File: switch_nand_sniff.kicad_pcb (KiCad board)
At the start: 2 copper layers, 24.9 x 11.4 mm, 7 parts, among them P1 CONN_02X15, P2 CONN_02X15, P3 CONN_01X02, P4 CONN_01X02

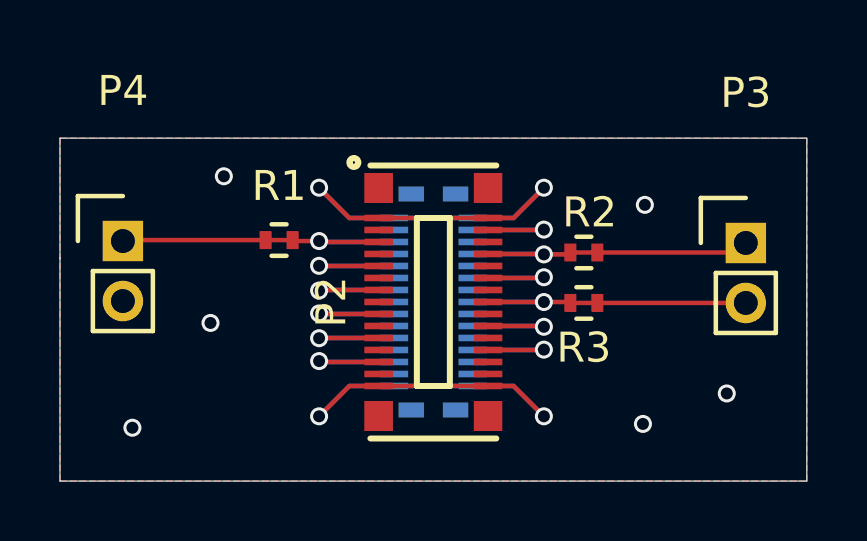
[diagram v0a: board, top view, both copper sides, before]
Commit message: Rev 1.1. Fixed resistor pad sizes, added thermal relief for ground plane.
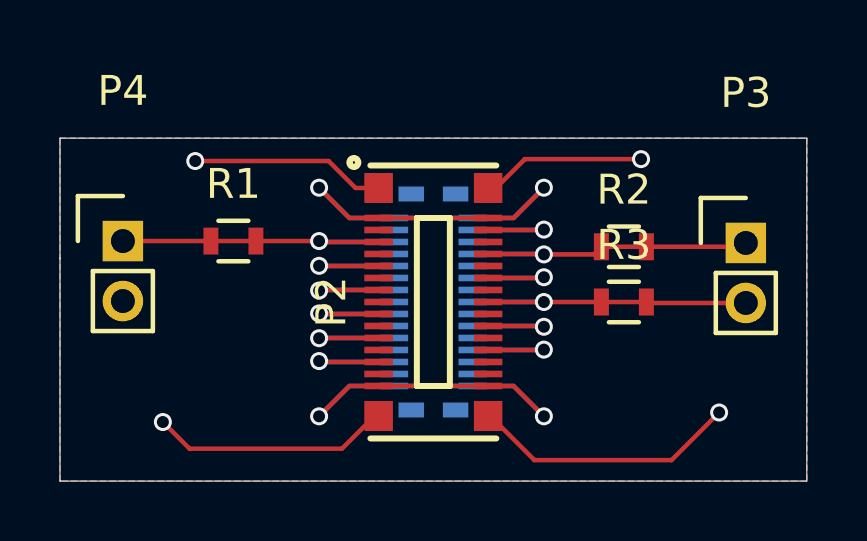
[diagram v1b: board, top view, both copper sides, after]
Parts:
- R1, R2, R3: footprint Resistors_SMD:R_0402 -> Resistors_SMD:R_0603
- moved R1 1.52 mm to (128.3, 133.0)
- moved R2 1.35 mm to (141.4, 133.2)
- moved R3 1.33 mm to (141.4, 135.0)
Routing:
- net GND: track 0.00 -> 29.4 mm, vias 0 -> 4
- net (no net): vias 6 -> 0

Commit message: Add sip-8. staging before rollback to find resistor desired.
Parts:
- removed R1, R2, R3: 0 Ohms, Resistors_SMD:R_0603
- P3, P4: value CONN_01X02 -> CONN_01X08; footprint Pin_Headers:Pin_Header_Straight_1x02_Pitch2.00mm -> switch:SIP-8
- moved P4 18.4 mm to (135.8, 147.6)
- moved P3 15.2 mm to (134.0, 122.9)
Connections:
- P1 pad 31: GND -> (no net)
- P2 pad 31: GND -> (no net)
- P3 pad 1: Net-(P1-Pad27) -> GND
- P3 pad 2: Net-(P1-Pad23) -> Net-(P1-Pad7)
- P4 pad 1: Net-(P1-Pad3) -> GND
- P4 pad 2: GND -> Net-(P1-Pad9)
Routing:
- net GND: track 29.4 -> 0.00 mm, vias 4 -> 0
- net Net-(P1-Pad27): track 11.6 -> 4.24 mm
- net Net-(P1-Pad23): track 11.0 -> 4.23 mm
- net Net-(P1-Pad3): track 11.1 -> 4.50 mm
- net (no net): track 0.00 -> 0.92 mm

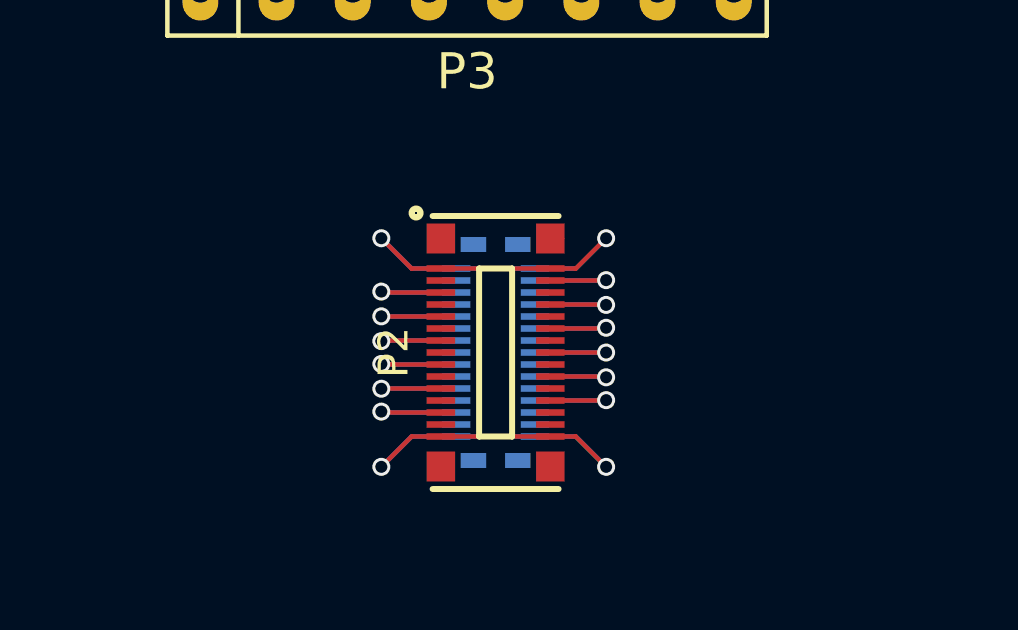
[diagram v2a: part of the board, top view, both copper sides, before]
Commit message: Added derefelection resistors, still needs matched-length routing.
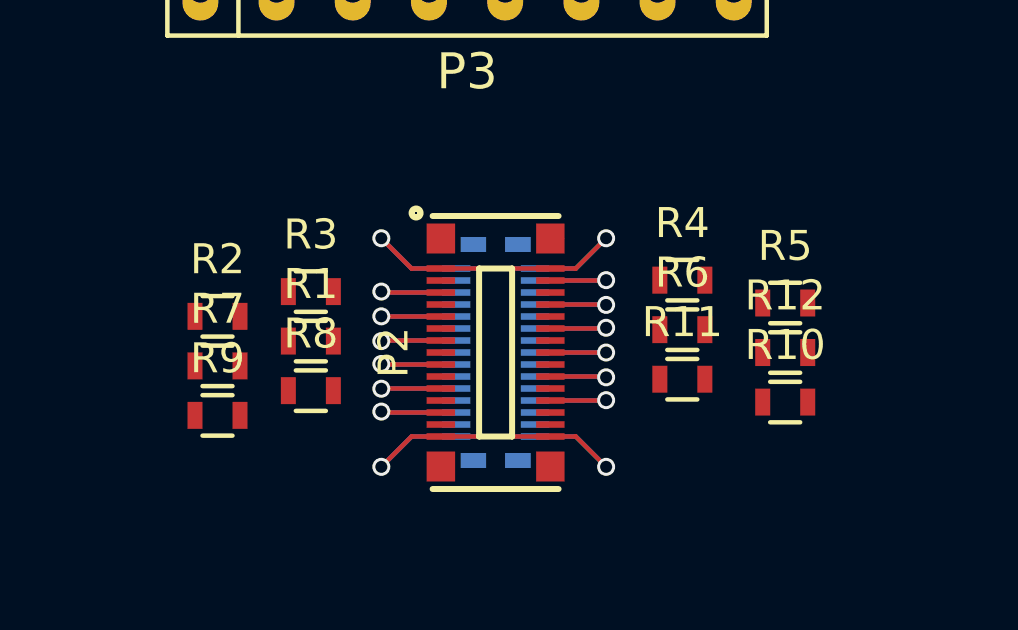
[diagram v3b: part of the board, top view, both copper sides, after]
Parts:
- added R1: 500 Ohms, Resistors_SMD:R_0603, F.Cu at (128.8, 134.6)
- added R10: 500 Ohms, Resistors_SMD:R_0603, F.Cu at (144.7, 136.7)
- added R11: 500 Ohms, Resistors_SMD:R_0603, F.Cu at (141.2, 135.9)
- added R12: 500 Ohms, Resistors_SMD:R_0603, F.Cu at (144.7, 135.0)
- added R2: 500 Ohms, Resistors_SMD:R_0603, F.Cu at (125.7, 133.8)
- added R3: 500 Ohms, Resistors_SMD:R_0603, F.Cu at (128.8, 133.0)
- added R4: 500 Ohms, Resistors_SMD:R_0603, F.Cu at (141.2, 132.6)
- added R5: 500 Ohms, Resistors_SMD:R_0603, F.Cu at (144.7, 133.3)
- added R6: 500 Ohms, Resistors_SMD:R_0603, F.Cu at (141.2, 134.2)
- added R7: 500 Ohms, Resistors_SMD:R_0603, F.Cu at (125.7, 135.4)
- added R8: 500 Ohms, Resistors_SMD:R_0603, F.Cu at (128.8, 136.3)
- added R9: 500 Ohms, Resistors_SMD:R_0603, F.Cu at (125.7, 137.1)

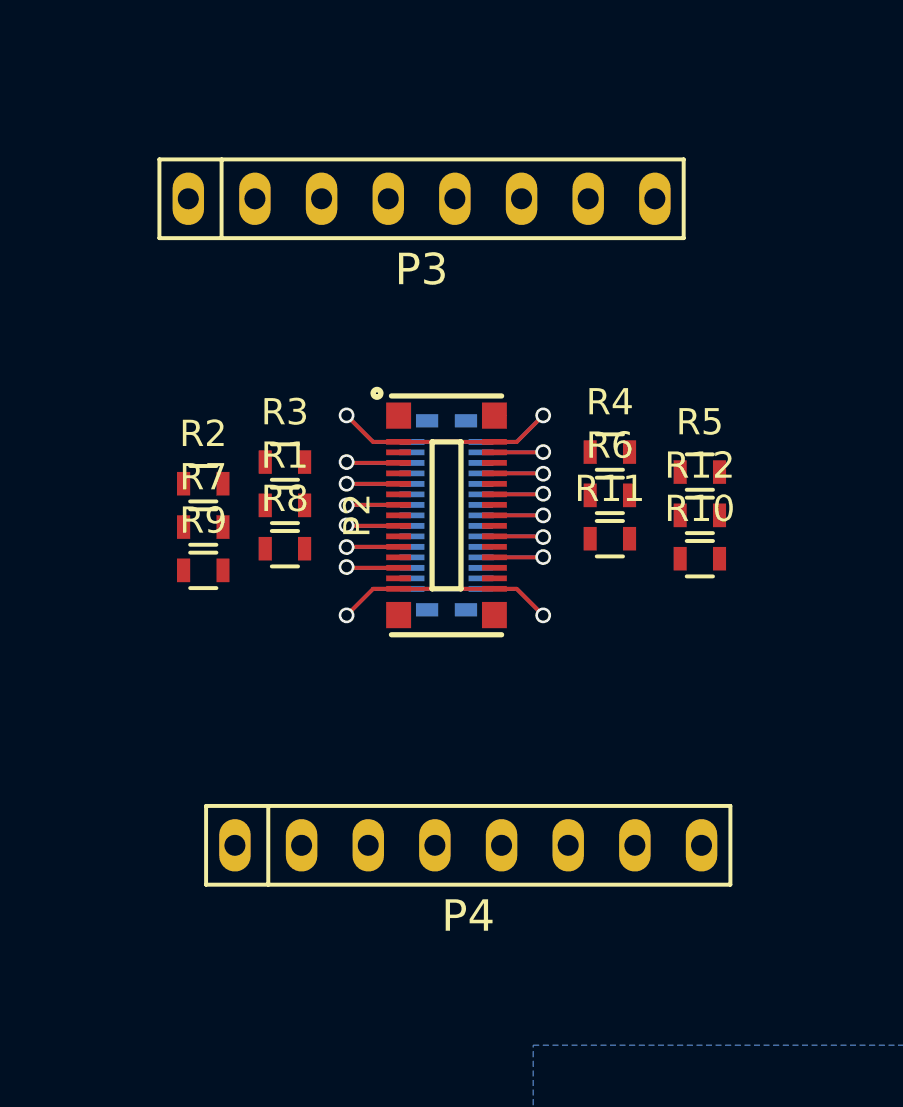
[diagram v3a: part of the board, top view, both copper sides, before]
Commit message: pre-routing. reorganized/normalized component placement. expanded power-line widths.
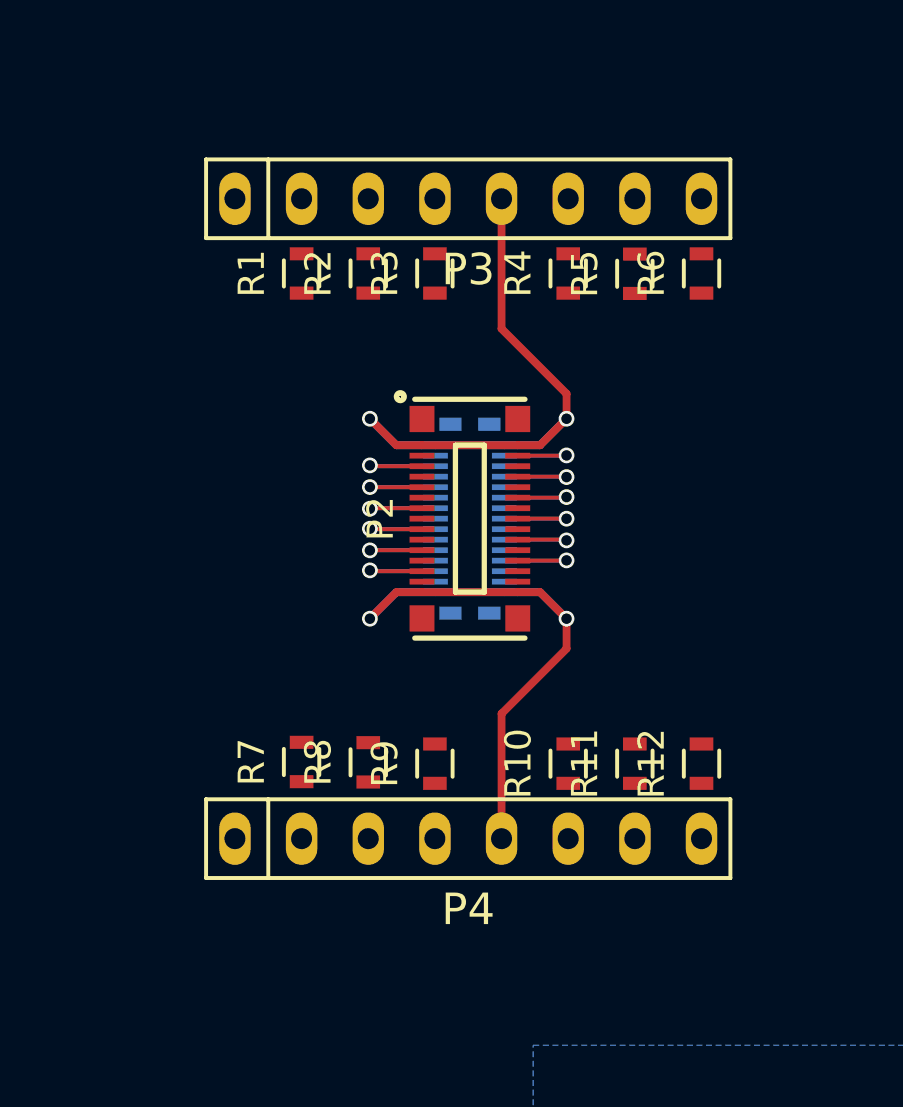
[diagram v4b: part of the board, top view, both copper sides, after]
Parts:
- moved R9 11.5 mm to (134.6, 144.5), turned to 90 degrees
- moved R2 10.2 mm to (132.0, 125.8), turned to 90 degrees
- moved R7 9.71 mm to (129.5, 144.4), turned to 90 degrees
- moved R12 9.46 mm to (144.7, 144.5), turned to 90 degrees
- moved R10 9.28 mm to (139.6, 144.5), turned to 90 degrees
- moved R3 9.18 mm to (134.6, 125.8), turned to 90 degrees
- moved R6 9.15 mm to (144.7, 125.8), turned to 90 degrees
- moved R1 8.86 mm to (129.5, 125.8), turned to 90 degrees
- moved R8 8.74 mm to (132.0, 144.4), turned to 90 degrees
- moved R11 8.63 mm to (142.2, 144.5), turned to 90 degrees
- moved R5 7.95 mm to (142.2, 125.8), turned to 90 degrees
- moved R4 6.99 mm to (139.6, 125.8), turned to 90 degrees
- moved P3 1.78 mm to (135.8, 122.9)
- moved P1 0.90 mm to (135.9, 135.1)
- moved P2 0.90 mm to (135.9, 135.1)
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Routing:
- net +3V3: track 16.7 -> 26.1 mm
- net Net-(P1-Pad1): track 16.7 -> 26.1 mm

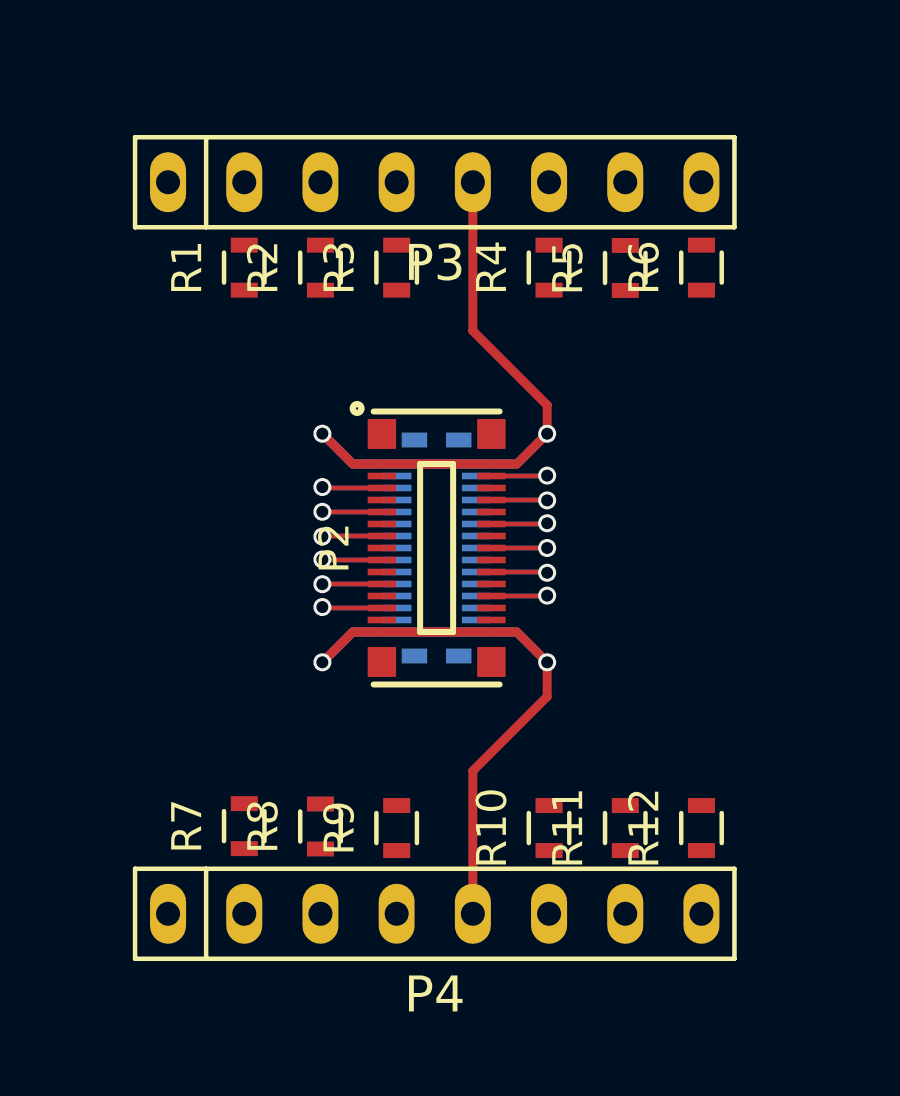
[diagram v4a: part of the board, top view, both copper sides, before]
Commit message: Routing finished. Needs length-matching + ground pour + edge cuts
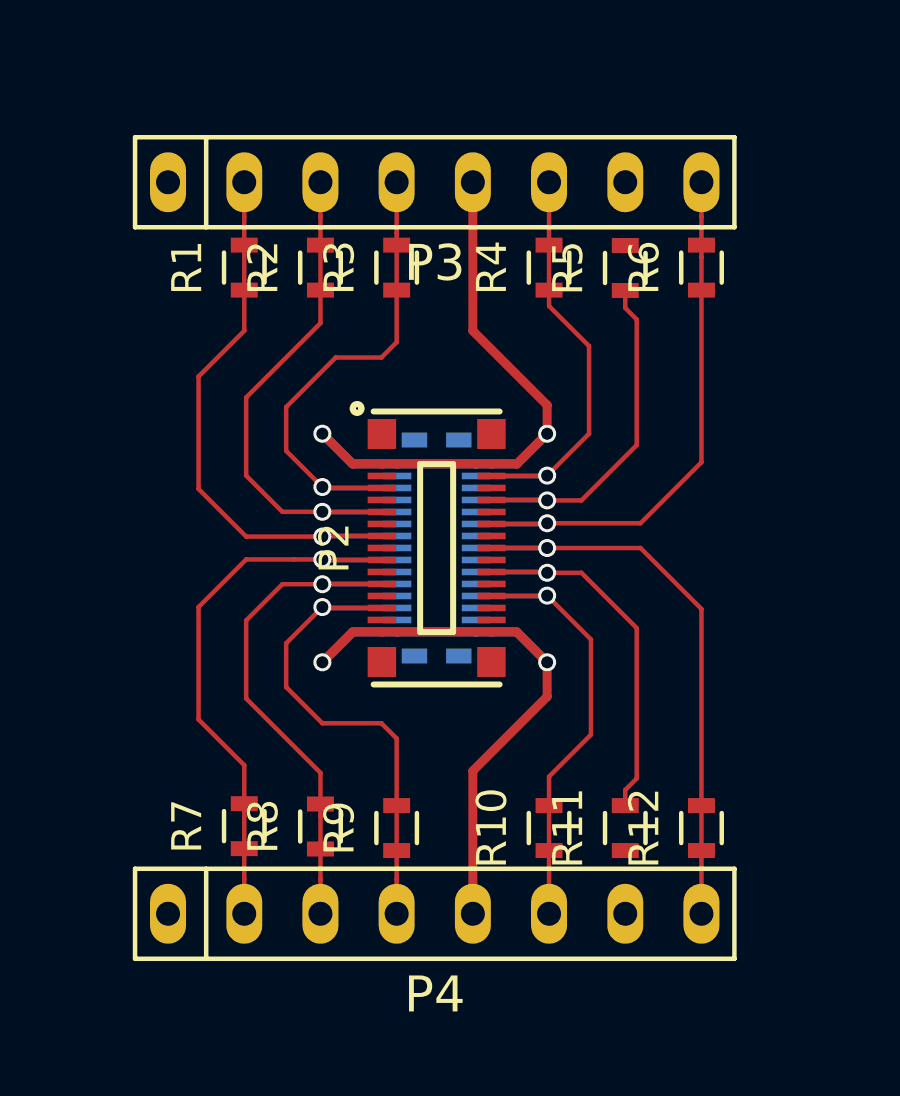
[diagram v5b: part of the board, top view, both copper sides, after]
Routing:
- net Net-(P1-Pad23): track 4.23 -> 20.4 mm
- net Net-(P1-Pad9): track 4.49 -> 20.1 mm
- net Net-(P1-Pad7): track 4.49 -> 20.1 mm
- net Net-(P1-Pad25): track 4.25 -> 19.6 mm
- net Net-(P1-Pad5): track 4.48 -> 18.3 mm
- net Net-(P1-Pad11): track 4.48 -> 18.3 mm
- net Net-(P1-Pad13): track 4.50 -> 17.9 mm
- net Net-(P1-Pad3): track 4.50 -> 17.6 mm
- net Net-(P1-Pad19): track 4.24 -> 16.0 mm
- net Net-(P1-Pad29): track 4.24 -> 15.1 mm
- net Net-(P1-Pad21): track 4.25 -> 14.1 mm
- net Net-(P1-Pad27): track 4.24 -> 13.3 mm

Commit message: Rev 2 done and production ready.
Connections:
- P1 pad 31: (no net) -> GND
- P2 pad 31: (no net) -> GND
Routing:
- net GND: track 0.00 -> 74.2 mm, vias 0 -> 20
- net Net-(P1-Pad27): track 13.3 -> 21.6 mm
- net Net-(P1-Pad21): track 14.1 -> 21.3 mm
- net Net-(P1-Pad29): track 15.1 -> 21.6 mm
- net Net-(P1-Pad19): track 16.0 -> 21.1 mm
- net Net-(P1-Pad3): track 17.6 -> 21.6 mm
- net Net-(P1-Pad13): track 17.9 -> 21.9 mm
- net Net-(P1-Pad5): track 18.3 -> 21.5 mm
- net Net-(P1-Pad11): track 18.3 -> 21.6 mm
- net Net-(P1-Pad25): track 19.6 -> 21.4 mm
- net Net-(P1-Pad7): track 20.1 -> 21.6 mm
- net Net-(P1-Pad9): track 20.1 -> 21.6 mm
- net Net-(P1-Pad23): track 20.4 -> 21.6 mm
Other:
- board size 24.9 x 11.4 mm -> 20.8 x 28.1 mm
